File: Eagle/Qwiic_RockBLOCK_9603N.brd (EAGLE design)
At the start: 50.8 x 50.8 mm, 68 parts, among them J1 SS4-10-3.50-X-D, J3 PTH, J6 ISP, J7 U.FL, Q1 DMG3415U-7, Q2 2N2222, U1 ATTINY84-ARDUINO, U2 LTC3225EDDB#TRMPBF

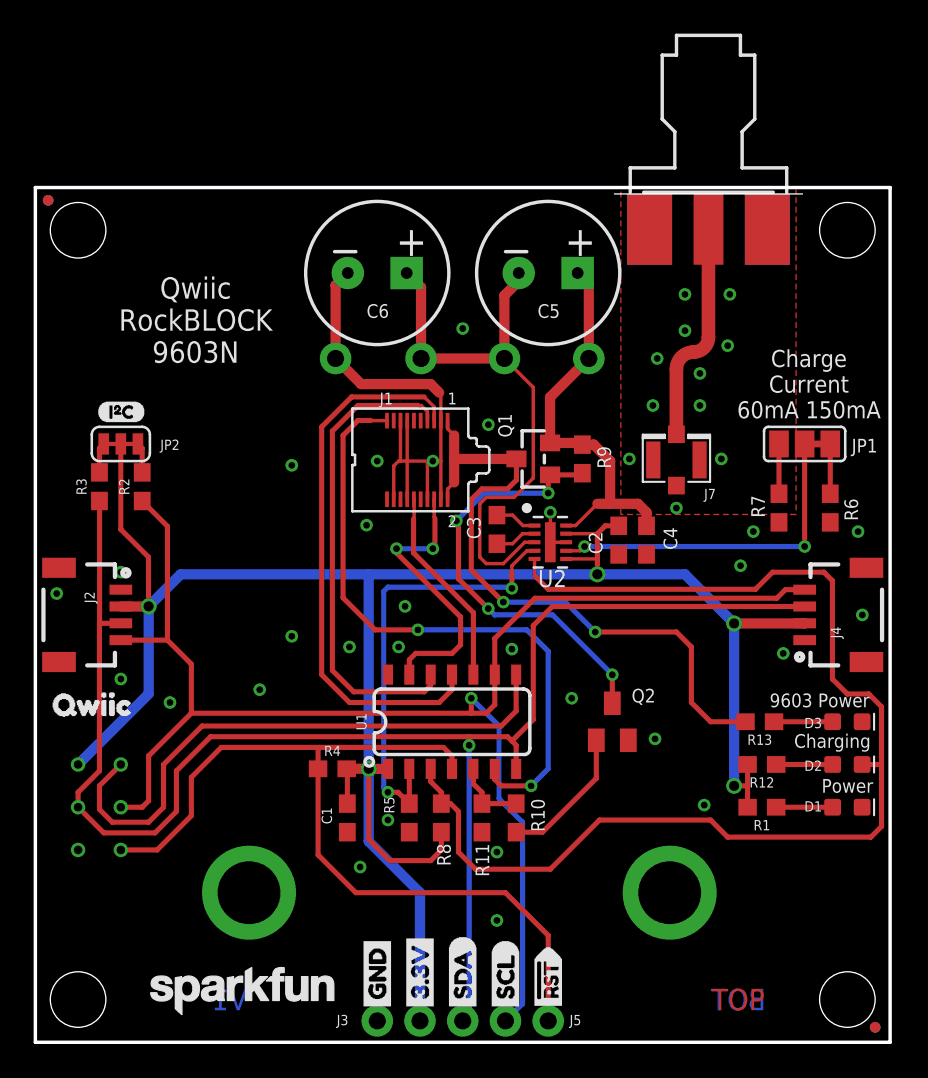
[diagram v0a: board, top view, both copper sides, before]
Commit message: Updated the PCB and included the Arduino code
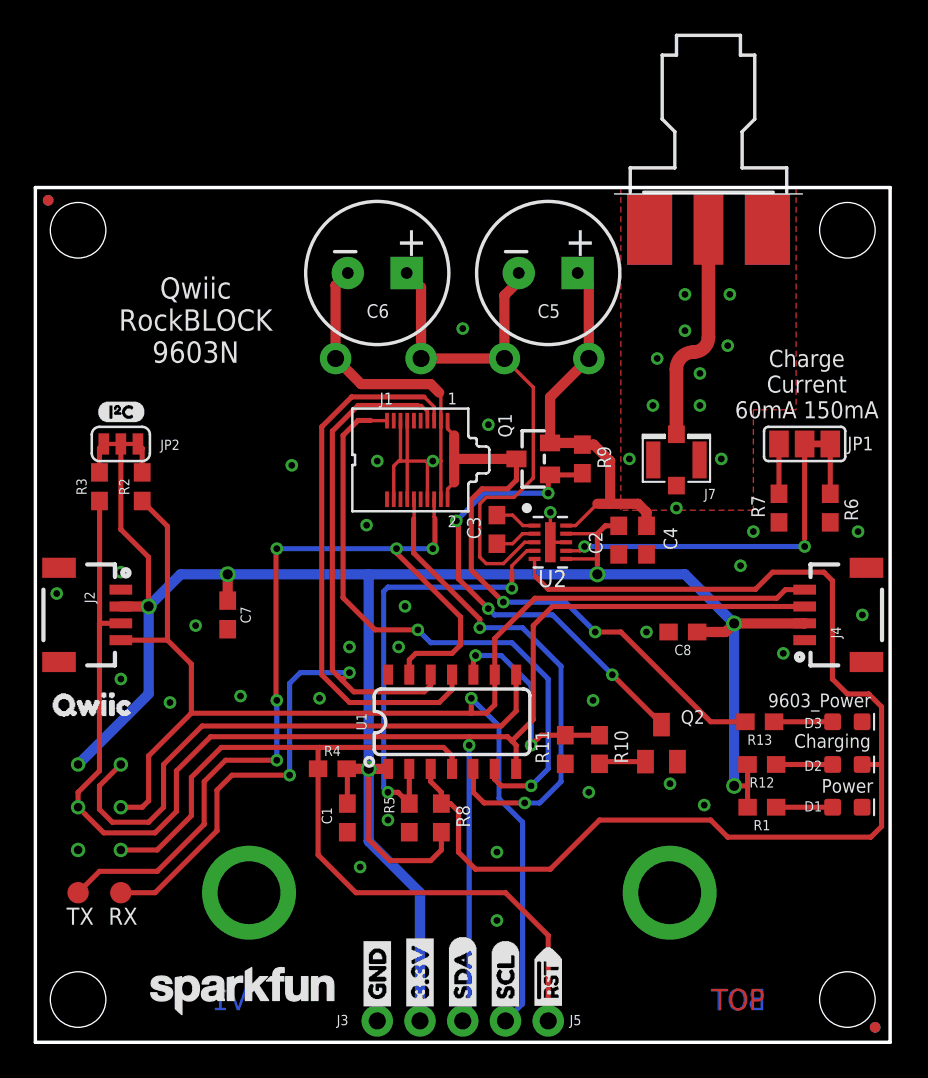
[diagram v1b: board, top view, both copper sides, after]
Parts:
- added C7: 10uF, SparkFun-Capacitors:0603
- added C8: 1.0uF, SparkFun-Capacitors:0603
- added RX, TX: TEST-POINT3X5, SparkFun-Connectors:PAD.03X.05
- moved R10 6.41 mm to (33.5, 17.4)
- moved R11 6.41 mm to (31.5, 17.4)
- moved Q2 3.19 mm to (37.2, 17.8)
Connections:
- net 3.3V: now also C7.1, C8.1
- net GND: now also C7.2, C8.2
- net PWR_EN: now also U1.10; no longer U1.5
- net RI: now also U1.5; no longer U1.10
- net RX(OUT): now also RX.P$1
- net TX(IN): now also TX.P$1
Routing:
- net TX(IN): track 16.8 -> 53.0 mm, vias 2 -> 5
- net RX(OUT): track 28.4 -> 52.6 mm, vias 0 -> 2
- net RI: track 11.9 -> 29.3 mm, vias 0 -> 2
- net PWR_EN: track 4.31 -> 13.1 mm, vias 0 -> 2
- net N$20: track 8.35 -> 2.79 mm
- net 3.3V: track 127.4 -> 131.4 mm, vias 5 -> 6
- net N$19: track 25.9 -> 28.4 mm
- net EXT_PWR: track 39.3 -> 37.3 mm
- net NA: track 37.5 -> 36.5 mm
- net GND: vias 40 -> 42
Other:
- board text added: "9603_Power"
- board text added: "RX"
- board text added: "TX"
- board text removed: "9603 Power"
